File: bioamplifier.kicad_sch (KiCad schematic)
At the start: 29 parts, among them J1 Conn_01x40_Pin, U1 ADS1299IPAG, U7 TPS73133DBV, U8 TPS73201DCQ

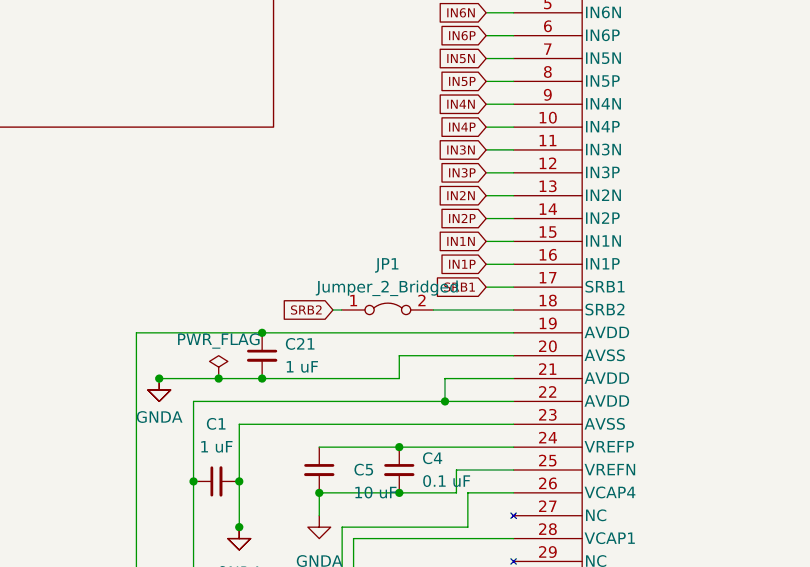
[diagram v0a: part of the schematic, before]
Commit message: redone analog inputs, adjusted all footprints to match real components, added library for potential implementation of 4 element capacitor arrays
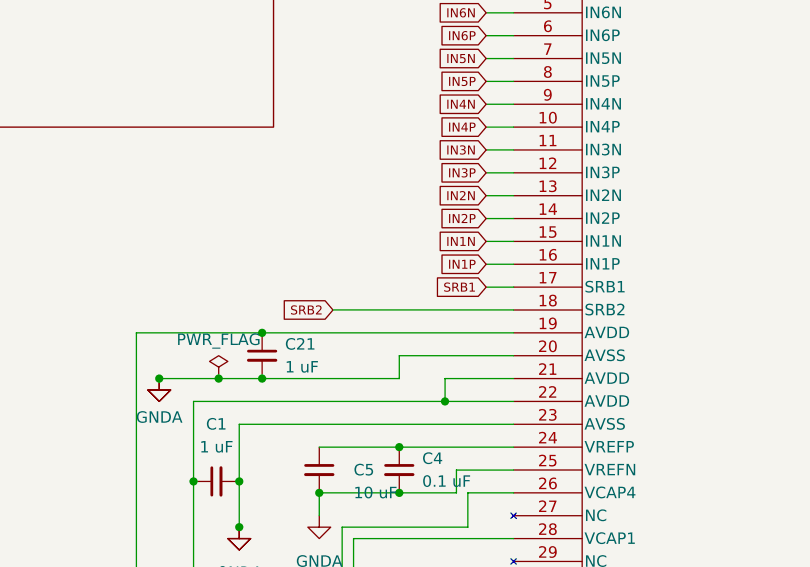
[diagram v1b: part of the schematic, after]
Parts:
- removed JP1: Jumper_2_Bridged, Jumper:SolderJumper-2_P1.3mm_Bridged2Bar_Pad1.0x1.5mm, symbol Jumper:Jumper_2_Bridged
- C1, C19, C2, C20, C21, C4, C6, C7: footprint Capacitor_SMD:C_0603_1608Metric -> Capacitor_SMD:C_0402_1005Metric
- C9: footprint Capacitor_SMD:C_0603_1608Metric -> Capacitor_SMD:C_0805_2012Metric
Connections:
- net SRB2: now also U1.18 (SRB2)
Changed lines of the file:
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@@
 	(wire
 		(pts
-			(xy 99.06 104.14) (xy 107.95 104.14)
-		)
-		(stroke
-			(width 0)
-			(type default)
-		)
-	)
-	(wire
-		(pts
 			(xy 209.296 35.814) (xy 214.376 35.814)
 		)
@@
 	(wire
 		(pts
-			(xy 87.884 104.14) (xy 88.9 104.14)
+			(xy 87.884 104.14) (xy 107.95 104.14)
 		)
 		(stroke
@@
 			)
 		)
-		(property "Footprint" "Capacitor_SMD:C_0603_1608Metric"
+		(property "Footprint" "Capacitor_SMD:C_0402_1005Metric"
 			(at 74.93 123.19 0)
 			(effects
@@
 			)
 		)
-		(property "Footprint" "Capacitor_SMD:C_0603_1608Metric"
+		(property "Footprint" "Capacitor_SMD:C_0402_1005Metric"
 			(at 240.03 104.14 0)
 			(effects
@@
 	)
 	(symbol
-		(lib_id "Jumper:Jumper_2_Bridged")
-		(at 93.98 104.14 0)
-		(unit 1)
-		(exclude_from_sim no)
-		(in_bom yes)
-		(on_board yes)
-		(dnp no)
-		(fields_autoplaced yes)
-		(property "Reference" "JP1"
-			(at 93.98 99.06 0)
-			(effects
-				(font
-					(size 1.27 1.27)
-				)
-			)
-		)
-		(property "Value" "Jumper_2_Bridged"
-			(at 93.98 101.6 0)
-			(effects
-				(font
-					(size 1.27 1.27)
-				)
-			)
-		)
-		(property "Footprint" "Jumper:SolderJumper-2_P1.3mm_Bridged2Bar_Pad1.0x1.5mm"
-			(at 93.98 104.14 0)
-			(effects
-				(font
-					(size 1.27 1.27)
-				)
-				(hide yes)
-			)
-		)
-		(property "Datasheet" "~"
-			(at 93.98 104.14 0)
-			(effects
-				(font
-					(size 1.27 1.27)
-				)
-				(hide yes)
-			)
-		)
-		(property "Description" ""
-			(at 93.98 104.14 0)
-			(effects
-				(font
-					(size 1.27 1.27)
-				)
-				(hide yes)
-			)
-		)
-		(pin "1"
-		)
-		(pin "2"
-		)
-		(instances
-			(project "bioamplifier"
-				(path "/59c54cdb-19a2-4654-a4c9-f1907d038780"
-					(reference "JP1")
-					(unit 1)
-				)
-			)
-		)
-	)
-	(symbol
 		(lib_id "power:GNDA")
 		(at 96.52 171.45 0)
@@
 			)
 		)
-		(property "Footprint" "Capacitor_SMD:C_0603_1608Metric"
+		(property "Footprint" "Capacitor_SMD:C_0402_1005Metric"
 			(at 222.25 86.36 0)
 			(effects
@@
 			)
 		)
-		(property "Footprint" "Capacitor_SMD:C_0603_1608Metric"
+		(property "Footprint" "Capacitor_SMD:C_0402_1005Metric"
 			(at 80.01 109.22 0)
 			(effects
@@
 			)
 		)
-		(property "Footprint" "Capacitor_SMD:C_0603_1608Metric"
+		(property "Footprint" "Capacitor_SMD:C_0402_1005Metric"
 			(at 234.95 86.36 0)
 			(effects
@@
 			)
 		)
-		(property "Footprint" "Capacitor_SMD:C_0603_1608Metric"
+		(property "Footprint" "Capacitor_SMD:C_0402_1005Metric"
 			(at 95.25 121.92 0)
 			(effects
@@
 			)
 		)
-		(property "Footprint" "Capacitor_SMD:C_0603_1608Metric"
+		(property "Footprint" "Capacitor_SMD:C_0402_1005Metric"
 			(at 212.09 119.38 0)
 			(effects
@@
 			)
 		)
-		(property "Footprint" "Capacitor_SMD:C_0603_1608Metric"
+		(property "Footprint" "Capacitor_SMD:C_0402_1005Metric"
 			(at 227.33 104.14 0)
 			(effects
@@
 			)
 		)
-		(property "Footprint" "Capacitor_SMD:C_0603_1608Metric"
+		(property "Footprint" "Capacitor_SMD:C_0805_2012Metric"
 			(at 90.17 161.29 0)
 			(effects
